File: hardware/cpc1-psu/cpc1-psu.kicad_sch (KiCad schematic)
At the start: 13 parts

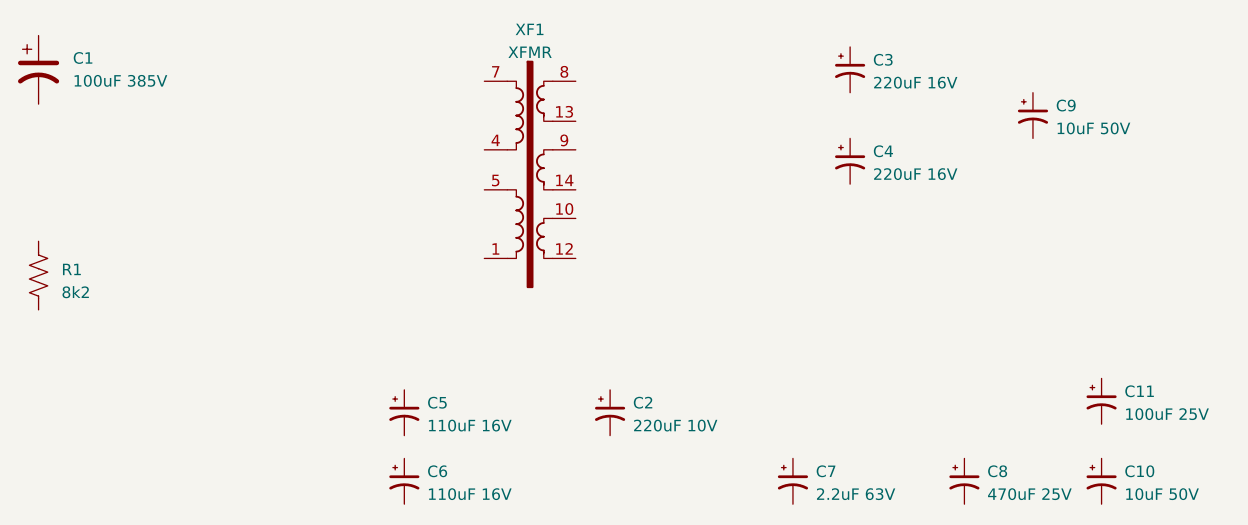
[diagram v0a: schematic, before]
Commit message: Fixed C3/C4 values
2200 uF! Doh!
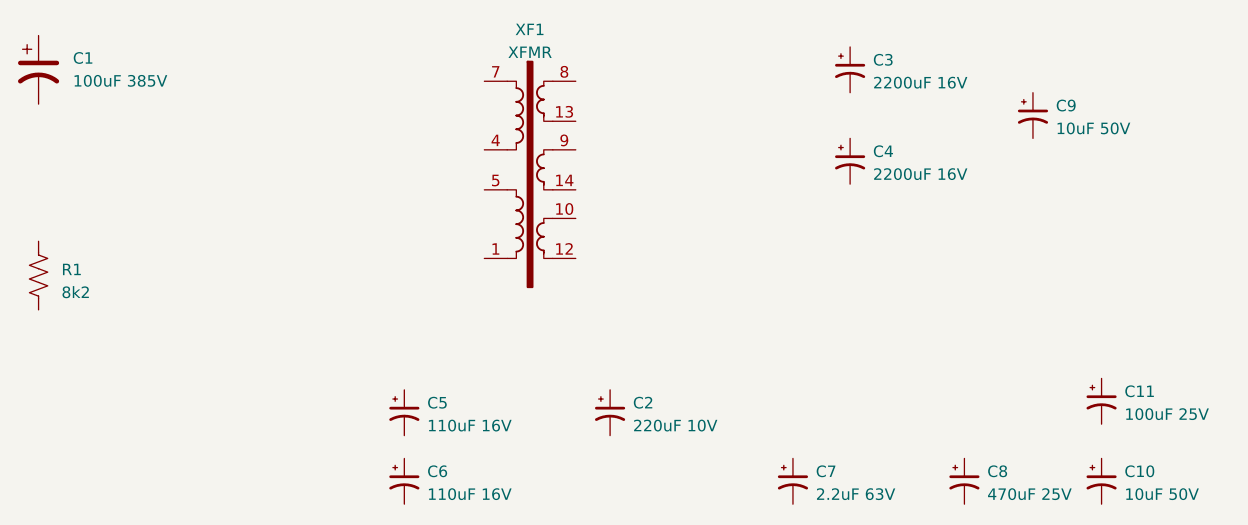
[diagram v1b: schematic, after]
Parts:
- C3, C4: value 220uF 16V -> 2200uF 16V; Farnell 2841894 -> 2508122
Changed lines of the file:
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@@
       (effects (font (size 1.27 1.27)) (justify left))
     )
-    (property "Value" "220uF 16V" (at 189.23 82.7532 0)
+    (property "Value" "2200uF 16V" (at 189.23 82.7532 0)
       (effects (font (size 1.27 1.27)) (justify left))
     )
@@
       (effects (font (size 1.27 1.27)) hide)
     )
-    (property "Datasheet" "https://4donline.ihs.com/images/VipMasterIC/IC/NICH/NICH-S-A0003527663/NICH-S-A0003527663-1.pdf?hkey=6D3A4C79FDBF58556ACFDE234799DDF0" (at 186.69 81.28 0)
+    (property "Datasheet" "https://www.farnell.com/datasheets/2820375.pdf" (at 186.69 81.28 0)
       (effects (font (size 1.27 1.27)) hide)
     )
-    (property "Farnell" "2841894" (at 186.69 81.28 0)
+    (property "Farnell" "2508122" (at 186.69 81.28 0)
       (effects (font (size 1.27 1.27)) hide)
     )
@@
       (effects (font (size 1.27 1.27)) (justify left))
     )
-    (property "Value" "220uF 16V" (at 189.23 72.5932 0)
+    (property "Value" "2200uF 16V" (at 189.23 72.5932 0)
       (effects (font (size 1.27 1.27)) (justify left))
     )
@@
       (effects (font (size 1.27 1.27)) hide)
     )
-    (property "Datasheet" "https://4donline.ihs.com/images/VipMasterIC/IC/NICH/NICH-S-A0003527663/NICH-S-A0003527663-1.pdf?hkey=6D3A4C79FDBF58556ACFDE234799DDF0" (at 186.69 71.12 0)
+    (property "Datasheet" "https://www.farnell.com/datasheets/2820375.pdf" (at 186.69 71.12 0)
       (effects (font (size 1.27 1.27)) hide)
     )
-    (property "Farnell" "2841894" (at 186.69 71.12 0)
+    (property "Farnell" "2508122" (at 186.69 71.12 0)
       (effects (font (size 1.27 1.27)) hide)
     )

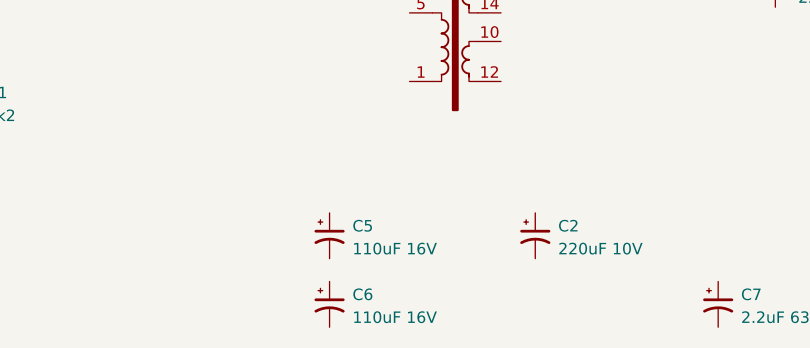
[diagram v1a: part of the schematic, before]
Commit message: Fixed C6 and C5 values
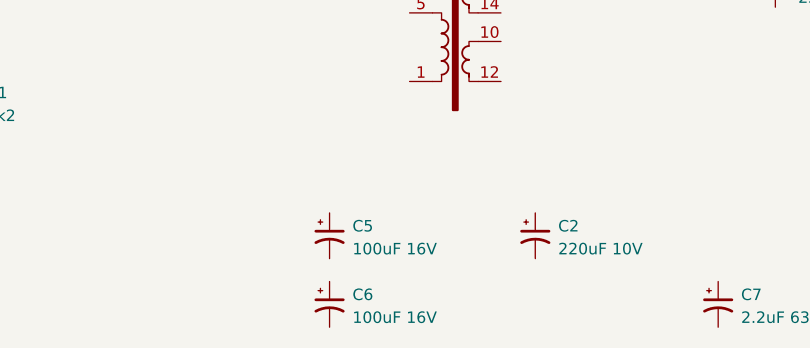
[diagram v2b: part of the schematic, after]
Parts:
- C5, C6: value 110uF 16V -> 100uF 16V
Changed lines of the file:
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@@
       (effects (font (size 1.27 1.27)) (justify left))
     )
-    (property "Value" "110uF 16V" (at 139.7 110.6932 0)
+    (property "Value" "100uF 16V" (at 139.7 110.6932 0)
       (effects (font (size 1.27 1.27)) (justify left))
     )
@@
       (effects (font (size 1.27 1.27)) (justify left))
     )
-    (property "Value" "110uF 16V" (at 139.7 118.3132 0)
+    (property "Value" "100uF 16V" (at 139.7 118.3132 0)
       (effects (font (size 1.27 1.27)) (justify left))
     )

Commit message: Changed part number
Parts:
- C5, C6: Farnell 3254073 -> 8767254
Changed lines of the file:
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@@
       (effects (font (size 1.27 1.27)) hide)
     )
-    (property "Datasheet" "https://www.farnell.com/datasheets/2885139.pdf" (at 137.16 109.22 0)
+    (property "Datasheet" "https://4donline.ihs.com/images/VipMasterIC/IC/PANA/PANA-S-A0009426292/PANA-S-A0009426292-1.pdf?hkey=6D3A4C79FDBF58556ACFDE234799DDF0" (at 137.16 109.22 0)
       (effects (font (size 1.27 1.27)) hide)
     )
-    (property "Farnell" "3254073" (at 137.16 109.22 0)
+    (property "Farnell" "8767254" (at 137.16 109.22 0)
       (effects (font (size 1.27 1.27)) hide)
     )
@@
       (effects (font (size 1.27 1.27)) hide)
     )
-    (property "Datasheet" "https://www.farnell.com/datasheets/2885139.pdf" (at 137.16 116.84 0)
+    (property "Datasheet" "https://4donline.ihs.com/images/VipMasterIC/IC/PANA/PANA-S-A0009426292/PANA-S-A0009426292-1.pdf?hkey=6D3A4C79FDBF58556ACFDE234799DDF0" (at 137.16 116.84 0)
       (effects (font (size 1.27 1.27)) hide)
     )
-    (property "Farnell" "3254073" (at 137.16 116.84 0)
+    (property "Farnell" "8767254" (at 137.16 116.84 0)
       (effects (font (size 1.27 1.27)) hide)
     )

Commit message: Change component (longer life)
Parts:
- C11: Farnell 2805620 -> 8767254
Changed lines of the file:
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@@
       (effects (font (size 1.27 1.27)) hide)
     )
-    (property "Datasheet" "https://4donline.ihs.com/images/VipMasterIC/IC/PANA/PANA-S-A0017226361/PANA-S-A0017230245-1.pdf?hkey=6D3A4C79FDBF58556ACFDE234799DDF0" (at 214.63 107.95 0)
+    (property "Datasheet" "https://4donline.ihs.com/images/VipMasterIC/IC/PANA/PANA-S-A0009426292/PANA-S-A0009426292-1.pdf?hkey=6D3A4C79FDBF58556ACFDE234799DDF0" (at 214.63 107.95 0)
       (effects (font (size 1.27 1.27)) hide)
     )
-    (property "Farnell" "2805620" (at 214.63 107.95 0)
+    (property "Farnell" "8767254" (at 214.63 107.95 0)
       (effects (font (size 1.27 1.27)) hide)
     )
